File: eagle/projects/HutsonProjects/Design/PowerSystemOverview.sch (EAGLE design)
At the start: 28 parts, among them U1 MCP7384XX, U3 MT3608, U4 LTC3531ES6-3_3

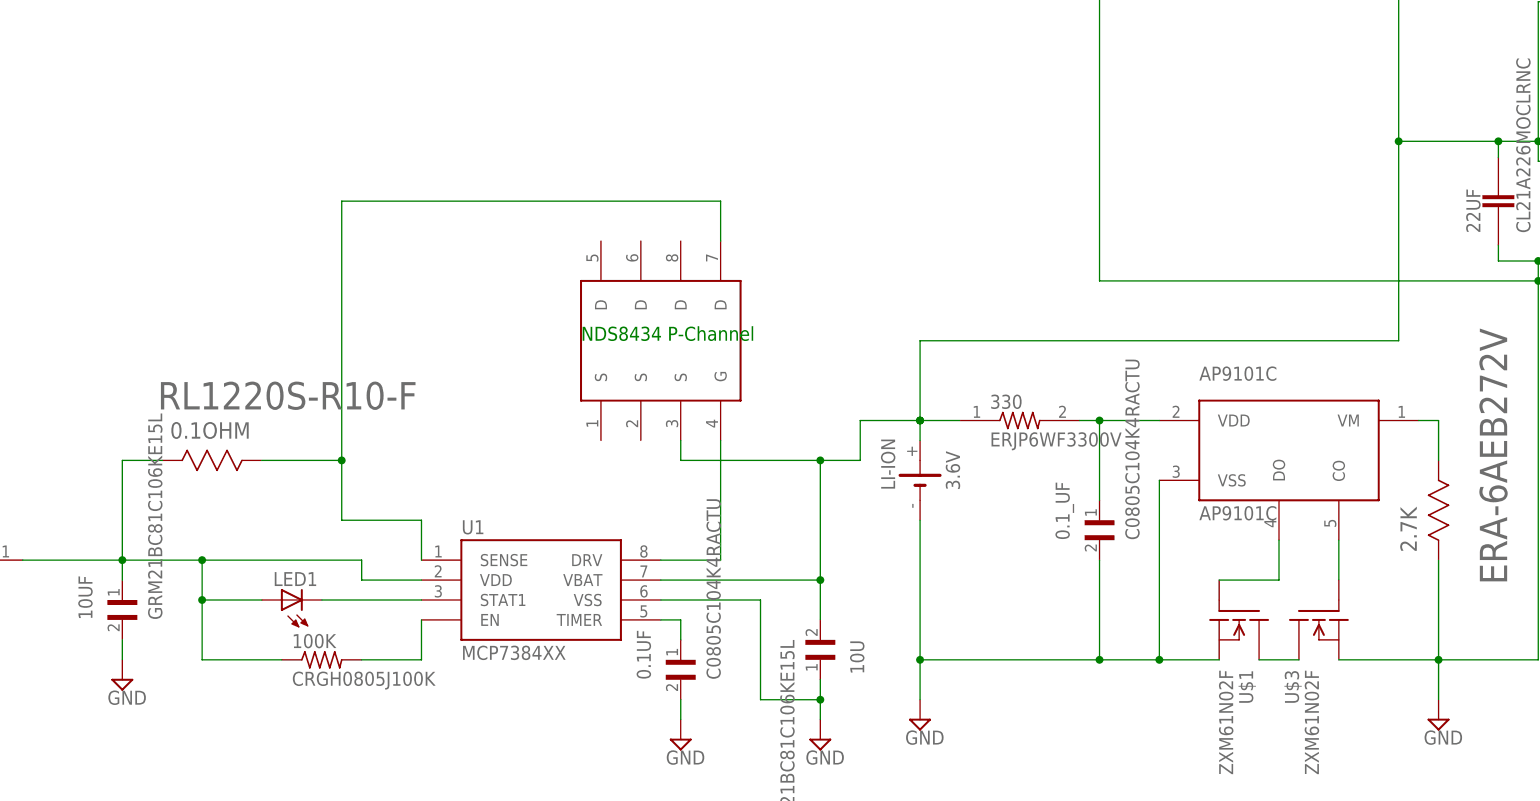
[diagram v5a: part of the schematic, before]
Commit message: SPDT added to circuit
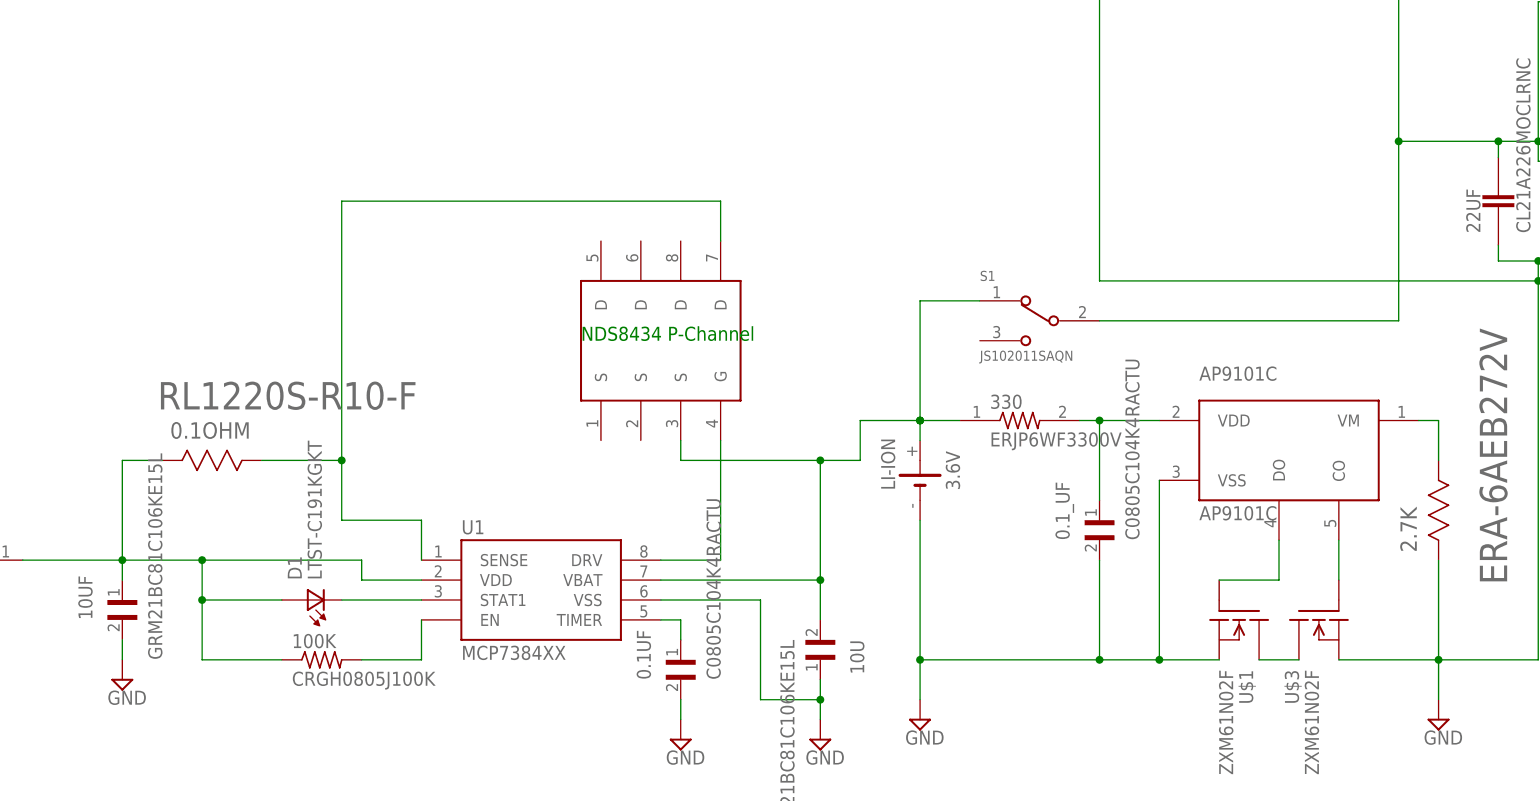
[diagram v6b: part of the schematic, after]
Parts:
- removed LED1: (no value), eagle-ltspice:LED_ESML0603
- added D1: LTST-C191KGKT, LTST-C191KGKT:LTST-C191KGKT
- added S1: JS102011SAQN, JS102011SAQN:JS102011SAQN
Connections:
- new net N$19: 10U.2, 330.1, LI-ION.+, S1.1, U$2.S@3, U1.VBAT
- net N$16: now also S1.2; no longer 10U.2, 330.1, LI-ION.+, U$2.S@3, U1.VBAT
- net N$3: now also D1.A2; no longer LED1.A
- net N$5: now also D1.K2; no longer LED1.C
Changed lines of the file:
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@@
 <part name="SUPPLY2" library="supply2" library_urn="urn:adsk.eagle:library:372" deviceset="GND" device=""/>
 <part name="SUPPLY3" library="supply2" library_urn="urn:adsk.eagle:library:372" deviceset="GND" device=""/>
-<part name="LED1" library="eagle-ltspice" library_urn="urn:adsk.eagle:library:217" deviceset="LED_E" device="SML0603" package3d_urn="urn:adsk.eagle:package:13315/1"/>
 <part name="U$2" library="NDS8434" deviceset="NDS8434" device=""/>
 <part name="U$1" library="ZXM61N02F" deviceset="ZXM61N02F" device=""/>
@@
 <part name="SUPPLY7" library="supply2" library_urn="urn:adsk.eagle:library:372" deviceset="GND" device=""/>
 <part name="2.2UF" library="C0805C225K4RACTU" deviceset="C0805C225K4RACTU" device=""/>
+<part name="D1" library="LTST-C191KGKT" deviceset="LTST-C191KGKT" device=""/>
+<part name="S1" library="JS102011SAQN" deviceset="JS102011SAQN" device=""/>
 </parts>
 <sheets>
@@
 <attribute name="VALUE" x="74.295" y="67.945" size="1.778" layer="96"/>
 </instance>
-<instance part="LED1" gate="G$1" x="7.62" y="88.9" smashed="yes" rot="R90">
-<attribute name="NAME" x="12.192" y="92.456" size="1.778" layer="95" rot="R180"/>
-<attribute name="VALUE" x="12.192" y="94.615" size="1.778" layer="96" rot="R180"/>
-</instance>
 <instance part="U$2" gate="G$1" x="55.88" y="121.92" smashed="yes" rot="R90"/>
 <instance part="U$1" gate="G$1" x="129.54" y="86.36" smashed="yes" rot="R270">
@@
 <instance part="10UF" gate="G$1" x="-12.7" y="86.36" smashed="yes" rot="R90">
 <attribute name="NAME" x="-16.51" y="86.36" size="1.778" layer="95" rot="R90"/>
-<attribute name="VALUE" x="-7.62" y="86.36" size="1.778" layer="96" rot="R90"/>
+<attribute name="VALUE" x="-7.62" y="81.28" size="1.778" layer="96" rot="R90"/>
 </instance>
 <instance part="10U" gate="G$1" x="76.2" y="83.82" smashed="yes" rot="R270">
@@
 <attribute name="VALUE" x="121.109640625" y="189.91431875" size="3.480709375" layer="96" ratio="10" rot="SR90"/>
 <attribute name="NAME" x="108.99125" y="194.66555" size="2.082909375" layer="95" ratio="10" rot="SR90"/>
+</instance>
+<instance part="D1" gate="G$1" x="12.7" y="88.9" smashed="yes" rot="R90">
+<attribute name="NAME" x="10.15498125" y="91.44501875" size="1.78151875" layer="95" rot="R90"/>
+<attribute name="VALUE" x="12.7" y="91.4425" size="1.77975" layer="96" rot="R90"/>
+</instance>
+<instance part="S1" gate="G$1" x="104.14" y="124.46" smashed="yes">
+<attribute name="NAME" x="96.517090625" y="129.541940625" size="1.270490625" layer="95"/>
+<attribute name="VALUE" x="96.511440625" y="119.374290625" size="1.27143125" layer="96"/>
 </instance>
 </instances>
@@
 <segment>
 <wire x1="-2.54" y1="93.98" x2="-2.54" y2="88.9" width="0.1524" layer="91"/>
-<pinref part="LED1" gate="G$1" pin="A"/>
-<wire x1="-2.54" y1="88.9" x2="5.08" y2="88.9" width="0.1524" layer="91"/>
 <wire x1="-2.54" y1="88.9" x2="-2.54" y2="81.28" width="0.1524" layer="91"/>
-<junction x="-2.54" y="88.9"/>
 <wire x1="-2.54" y1="93.98" x2="17.78" y2="93.98" width="0.1524" layer="91"/>
 <wire x1="17.78" y1="93.98" x2="17.78" y2="91.44" width="0.1524" layer="91"/>
@@
 <pinref part="10UF" gate="G$1" pin="1"/>
 <wire x1="-12.7" y1="93.98" x2="-12.7" y2="91.44" width="0.1524" layer="91"/>
+<pinref part="D1" gate="G$1" pin="A2"/>
+<wire x1="-2.54" y1="88.9" x2="7.62" y2="88.9" width="0.1524" layer="91"/>
+<junction x="-2.54" y="88.9"/>
 </segment>
 </net>
@@
 </segment>
 </net>
-<net name="N$5" class="0">
-<segment>
-<pinref part="LED1" gate="G$1" pin="C"/>
-<pinref part="U1" gate="G$1" pin="STAT1"/>
-<wire x1="12.7" y1="88.9" x2="25.4" y2="88.9" width="0.1524" layer="91"/>
-</segment>
-</net>
 <net name="N$1" class="0">
 <segment>
@@
 <net name="N$16" class="0">
 <segment>
-<pinref part="U$2" gate="G$1" pin="S@3"/>
-<wire x1="58.42" y1="106.68" x2="58.42" y2="109.22" width="0.1524" layer="91"/>
-<wire x1="58.42" y1="106.68" x2="76.2" y2="106.68" width="0.1524" layer="91"/>
-<junction x="76.2" y="106.68"/>
-<wire x1="76.2" y1="91.44" x2="76.2" y2="106.68" width="0.1524" layer="91"/>
-<pinref part="U1" gate="G$1" pin="VBAT"/>
-<wire x1="55.88" y1="91.44" x2="76.2" y2="91.44" width="0.1524" layer="91"/>
-<wire x1="76.2" y1="106.68" x2="81.28" y2="106.68" width="0.1524" layer="91"/>
-<wire x1="81.28" y1="106.68" x2="81.28" y2="111.76" width="0.1524" layer="91"/>
-<pinref part="LI-ION" gate="G$1" pin="+"/>
-<wire x1="88.9" y1="109.22" x2="88.9" y2="111.76" width="0.1524" layer="91"/>
-<wire x1="88.9" y1="111.76" x2="88.9" y2="121.92" width="0.1524" layer="91"/>
-<wire x1="88.9" y1="121.92" x2="149.86" y2="121.92" width="0.1524" layer="91"/>
 <pinref part="L1" gate="G$1" pin="1"/>
 <wire x1="167.64" y1="165.1" x2="172.72" y2="165.1" width="0.1524" layer="91"/>
@@
 <wire x1="149.86" y1="147.32" x2="162.56" y2="147.32" width="0.1524" layer="91"/>
 <wire x1="162.56" y1="147.32" x2="167.64" y2="147.32" width="0.1524" layer="91"/>
-<wire x1="149.86" y1="121.92" x2="149.86" y2="147.32" width="0.1524" layer="91"/>
-<wire x1="81.28" y1="111.76" x2="88.9" y2="111.76" width="0.1524" layer="91"/>
-<junction x="88.9" y="111.76"/>
 <wire x1="149.86" y1="147.32" x2="149.86" y2="167.64" width="0.1524" layer="91"/>
 <wire x1="149.86" y1="167.64" x2="83.82" y2="167.64" width="0.1524" layer="91"/>
-<junction x="149.86" y="147.32"/>
 <pinref part="U4" gate="A" pin="VIN"/>
 <wire x1="127" y1="213.36" x2="132.08" y2="213.36" width="0.1524" layer="91"/>
@@
 <wire x1="83.82" y1="167.64" x2="83.82" y2="213.36" width="0.1524" layer="91"/>
 <wire x1="83.82" y1="213.36" x2="111.76" y2="213.36" width="0.1524" layer="91"/>
-<pinref part="330" gate="G$1" pin="1"/>
 <wire x1="111.76" y1="213.36" x2="127" y2="213.36" width="0.1524" layer="91"/>
-<wire x1="88.9" y1="111.76" x2="93.98" y2="111.76" width="0.1524" layer="91"/>
-<junction x="88.9" y="111.76"/>
-<pinref part="10U" gate="G$1" pin="2"/>
-<wire x1="76.2" y1="91.44" x2="76.2" y2="86.36" width="0.1524" layer="91"/>
-<junction x="76.2" y="91.44"/>
 <pinref part="22UF" gate="G$1" pin="2"/>
 <wire x1="162.56" y1="147.32" x2="162.56" y2="145.288" width="0.1524" layer="91"/>
@@
 <wire x1="111.76" y1="213.36" x2="111.76" y2="203.2" width="0.1524" layer="91"/>
 <junction x="111.76" y="213.36"/>
+<pinref part="S1" gate="G$1" pin="2"/>
+<wire x1="111.76" y1="124.46" x2="149.86" y2="124.46" width="0.1524" layer="91"/>
+<wire x1="149.86" y1="124.46" x2="149.86" y2="147.32" width="0.1524" layer="91"/>
+<junction x="149.86" y="147.32"/>
 </segment>
 </net>
@@
 </segment>
 </net>
+<net name="N$5" class="0">
+<segment>
+<pinref part="D1" gate="G$1" pin="K2"/>
+<pinref part="U1" gate="G$1" pin="STAT1"/>
+<wire x1="15.24" y1="88.9" x2="25.4" y2="88.9" width="0.1524" layer="91"/>
+</segment>
+</net>
+<net name="N$19" class="0">
+<segment>
+<pinref part="10U" gate="G$1" pin="2"/>
+<pinref part="330" gate="G$1" pin="1"/>
+<pinref part="LI-ION" gate="G$1" pin="+"/>
+<wire x1="88.9" y1="109.22" x2="88.9" y2="111.76" width="0.1524" layer="91"/>
+<wire x1="88.9" y1="111.76" x2="88.9" y2="127" width="0.1524" layer="91"/>
+<junction x="88.9" y="111.76"/>
+<wire x1="88.9" y1="111.76" x2="93.98" y2="111.76" width="0.1524" layer="91"/>
+<junction x="88.9" y="111.76"/>
+<wire x1="81.28" y1="111.76" x2="88.9" y2="111.76" width="0.1524" layer="91"/>
+<wire x1="81.28" y1="106.68" x2="81.28" y2="111.76" width="0.1524" layer="91"/>
+<pinref part="U$2" gate="G$1" pin="S@3"/>
+<wire x1="58.42" y1="106.68" x2="58.42" y2="109.22" width="0.1524" layer="91"/>
+<wire x1="58.42" y1="106.68" x2="76.2" y2="106.68" width="0.1524" layer="91"/>
+<junction x="76.2" y="106.68"/>
+<wire x1="76.2" y1="106.68" x2="81.28" y2="106.68" width="0.1524" layer="91"/>
+<wire x1="76.2" y1="91.44" x2="76.2" y2="106.68" width="0.1524" layer="91"/>
+<wire x1="76.2" y1="91.44" x2="76.2" y2="86.36" width="0.1524" layer="91"/>
+<junction x="76.2" y="91.44"/>
+<pinref part="U1" gate="G$1" pin="VBAT"/>
+<wire x1="55.88" y1="91.44" x2="76.2" y2="91.44" width="0.1524" layer="91"/>
+<pinref part="S1" gate="G$1" pin="1"/>
+<wire x1="88.9" y1="127" x2="96.52" y2="127" width="0.1524" layer="91"/>
+</segment>
+</net>
